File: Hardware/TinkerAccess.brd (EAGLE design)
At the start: 65 x 56.5 mm, 45 parts, among them Q1 500mA/300V, Q2 310mA/60V/1.6Ω, U1 SOIC-8SOIC-8

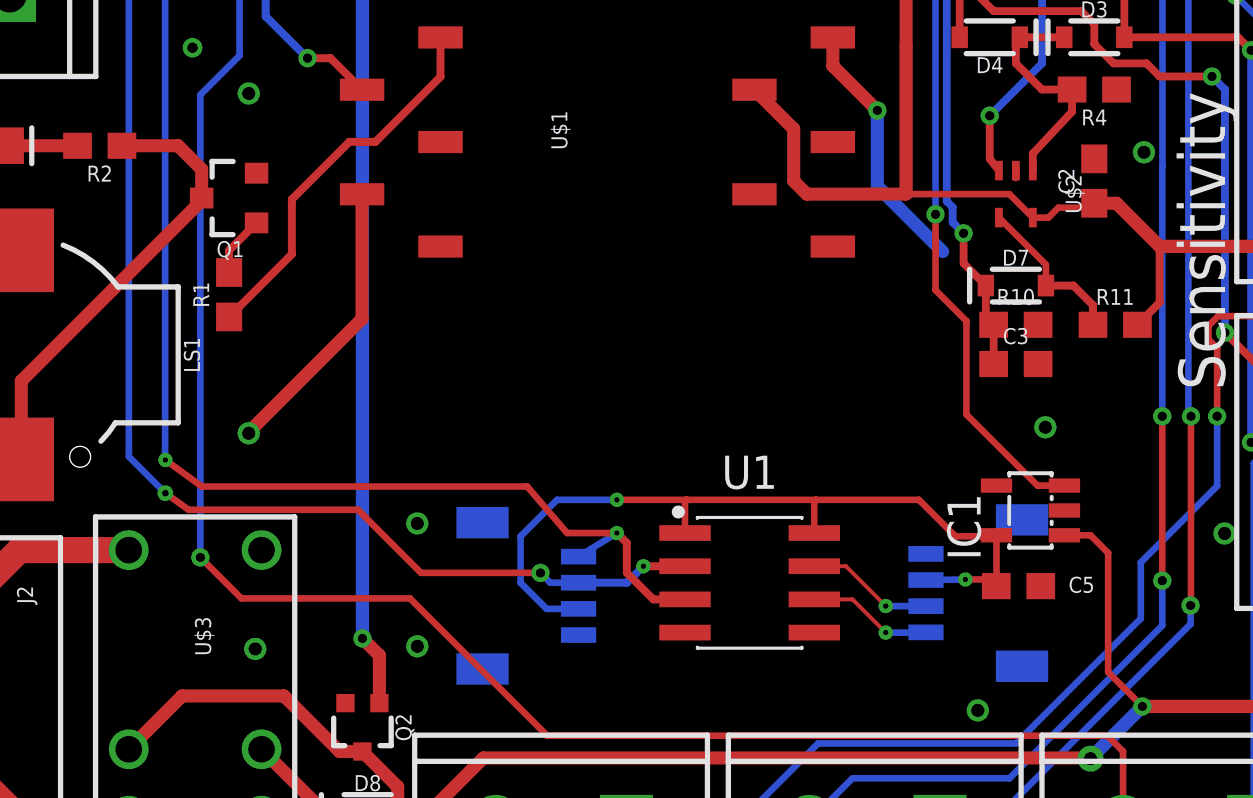
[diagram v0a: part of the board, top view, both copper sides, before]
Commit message: TinkerBoard Update
Fixed Drill Hole size to match Design rules.
Fixed Pad sizes.
Fixed AirWires.
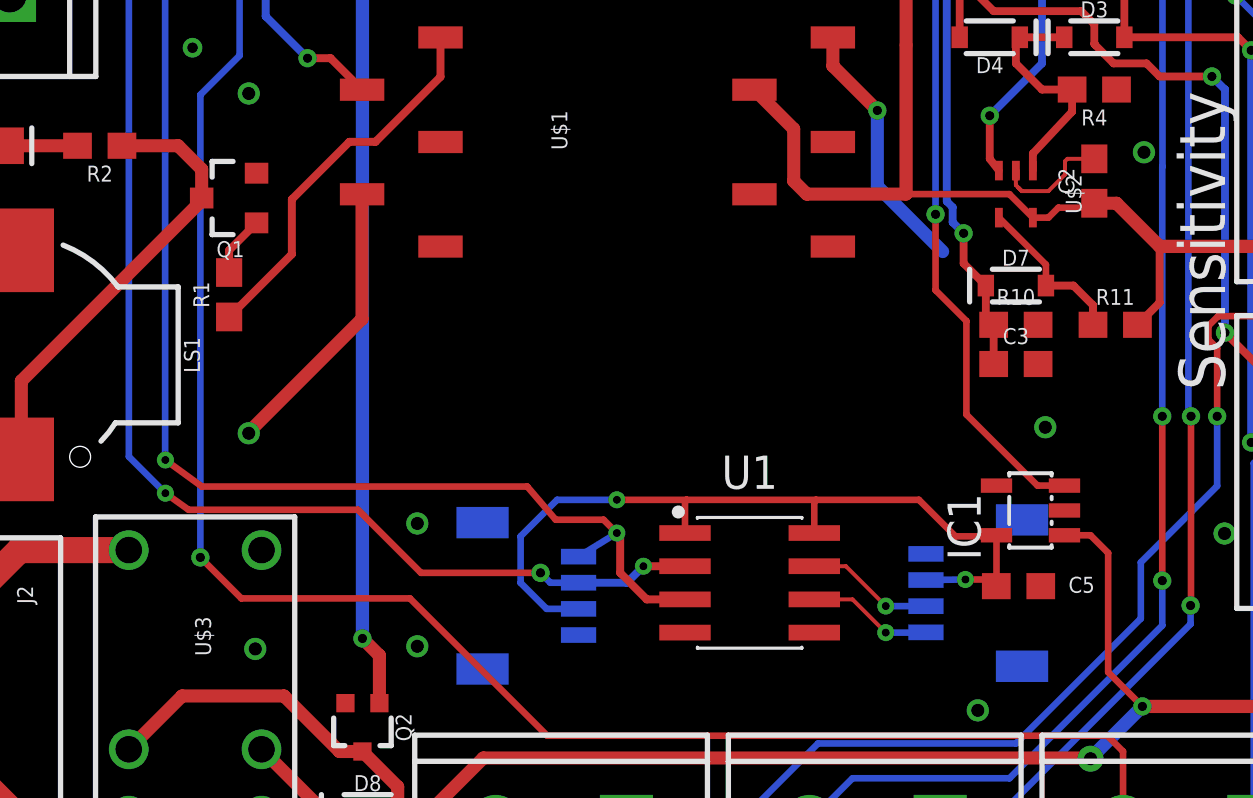
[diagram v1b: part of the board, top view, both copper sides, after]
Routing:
- net GND: track 21.2 -> 25.8 mm
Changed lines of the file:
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@@
 <setting verticaltext="up"/>
 </settings>
-<grid distance="5" unitdist="mil" unit="mil" style="lines" multiple="1" display="no" altdistance="5" altunitdist="mil" altunit="mil"/>
+<grid distance="5" unitdist="mil" unit="mm" style="lines" multiple="1" display="no" altdistance="5" altunitdist="mil" altunit="mm"/>
 <layers>
 <layer number="1" name="Top" color="4" fill="1" visible="yes" active="yes"/>
@@
 </class>
 </classes>
-<designrules name="LaenPCBOrder">
+<designrules name="LaenPCBOrder *">
 <description language="de">&lt;b&gt;EAGLE Design Rules&lt;/b&gt;
 &lt;p&gt;
@@
 <param name="mdSmdStop" value="0mil"/>
 <param name="msWidth" value="6mil"/>
-<param name="msDrill" value="13mil"/>
+<param name="msDrill" value="0.3mm"/>
 <param name="msMicroVia" value="13mil"/>
 <param name="msBlindViaRatio" value="0.5"/>
@@
 <signal name="BSDA">
 <contactref element="J9" pad="3"/>
-<via x="41.021" y="15.24" extent="1-16" drill="0.2"/>
+<via x="41.021" y="15.24" extent="1-16" drill="0.3"/>
 <contactref element="U1" pad="7"/>
 <wire x1="38.2874" y1="16.764" x2="39.497" y2="16.764" width="0.1524" layer="1"/>
@@
 <signal name="BSCL">
 <contactref element="J9" pad="4"/>
-<via x="41.021" y="14.224" extent="1-16" drill="0.2"/>
+<via x="41.021" y="14.224" extent="1-16" drill="0.3"/>
 <wire x1="42.549" y1="14.224" x2="42.56" y2="14.235" width="0.254" layer="16"/>
 <contactref element="U1" pad="6"/>
@@
 <via x="47.1248" y="22.0798" extent="1-16" drill="0.5" diameter="0.55" shape="square"/>
 <contactref element="U1" pad="4"/>
-<wire x1="52.6" y1="45.7" x2="56.63" y2="51.23" width="0" layer="19" extent="1-1"/>
-<wire x1="52.6" y1="44" x2="52.6" y2="45.7" width="0" layer="19" extent="1-1"/>
-<wire x1="52.6" y1="42.3" x2="52.6" y2="44" width="0" layer="19" extent="1-1"/>
-<wire x1="49.85" y1="43" x2="52.6" y2="42.3" width="0" layer="19" extent="1-1"/>
-<wire x1="54.9" y1="40.6" x2="52.6" y2="42.3" width="0" layer="19" extent="1-1"/>
-<wire x1="44.9" y1="45.6" x2="49.85" y2="43" width="0" layer="19" extent="1-1"/>
-<wire x1="49.85" y1="35" x2="54.9" y2="40.6" width="0" layer="19" extent="1-1"/>
-<wire x1="50.9" y1="32.6" x2="49.85" y2="35" width="0" layer="19" extent="1-1"/>
-<wire x1="49" y1="32.35" x2="50.9" y2="32.6" width="0" layer="19" extent="1-1"/>
-<wire x1="46" y1="31.9" x2="49" y2="32.35" width="0" layer="19" extent="1-1"/>
-<wire x1="43.2" y1="28.8" x2="46" y2="31.63979375" width="0" layer="19" extent="1-16"/>
-<wire x1="46.85" y1="26" x2="43.2" y2="28.8" width="0" layer="19" extent="1-16"/>
-<wire x1="46.85" y1="24.5" x2="46.85" y2="26" width="0" layer="19" extent="1-1"/>
-<wire x1="47.1248" y1="22.0798" x2="46.85" y2="24.5" width="0" layer="19" extent="1-1"/>
-<wire x1="47.8583" y1="18.8976" x2="47.1248" y2="22.0798" width="0" layer="19" extent="1-1"/>
-<wire x1="46.951" y1="16.002" x2="47.8583" y2="18.8976" width="0" layer="19" extent="1-1"/>
-<wire x1="42.56" y1="17.235" x2="46.951" y2="16.002" width="0" layer="19" extent="1-16"/>
-<wire x1="44.543" y1="11.249" x2="46.951" y2="16.002" width="0" layer="19" extent="1-1"/>
-<wire x1="53.9828" y1="18.0158" x2="47.8583" y2="18.8976" width="0" layer="19" extent="1-1"/>
-<wire x1="58.9" y1="16.6" x2="53.9828" y2="18.0158" width="0" layer="19" extent="1-1"/>
-<wire x1="60" y1="20" x2="58.9" y2="16.6" width="0" layer="19" extent="1-1"/>
-<wire x1="60.9" y1="24.6" x2="60" y2="20" width="0" layer="19" extent="1-1"/>
-<wire x1="49.01" y1="53.77" x2="56.63" y2="51.23" width="0" layer="19" extent="1-1"/>
-<wire x1="43.93" y1="53.77" x2="49.01" y2="53.77" width="0" layer="19" extent="1-1"/>
-<wire x1="38.85" y1="51.23" x2="43.93" y2="53.77" width="0" layer="19" extent="1-1"/>
-<wire x1="31.23" y1="53.77" x2="38.85" y2="51.23" width="0" layer="19" extent="1-1"/>
-<wire x1="23.61" y1="53.77" x2="31.23" y2="53.77" width="0" layer="19" extent="1-1"/>
-<wire x1="18.53" y1="51.23" x2="23.61" y2="53.77" width="0" layer="19" extent="1-1"/>
-<wire x1="13.45" y1="53.77" x2="18.53" y2="51.23" width="0" layer="19" extent="1-1"/>
-<wire x1="14.9" y1="45.6" x2="18.53" y2="51.23" width="0" layer="19" extent="1-1"/>
-<wire x1="17.35" y1="41" x2="14.9" y2="45.6" width="0" layer="19" extent="1-1"/>
-<wire x1="12.8" y1="40.3" x2="17.35" y2="41" width="0" layer="19" extent="1-1"/>
-<wire x1="14.5" y1="36.6" x2="12.8" y2="40.3" width="0" layer="19" extent="1-1"/>
-<wire x1="16.65" y1="34.85" x2="14.5" y2="36.6" width="0" layer="19" extent="1-1"/>
-<wire x1="16.95" y1="31.8" x2="16.65" y2="34.85" width="0" layer="19" extent="1-1"/>
-<wire x1="20.9868" y1="30.9934" x2="16.95" y2="31.8" width="0" layer="19" extent="1-1"/>
-<wire x1="16.65" y1="21.85" x2="16.6" y2="21.841" width="0" layer="19" extent="1-1"/>
-<wire x1="7.5" y1="38.6" x2="12.8" y2="40.3" width="0" layer="19" extent="1-1"/>
-<wire x1="23.1" y1="18.4" x2="16.65" y2="21.85" width="0" layer="19" extent="1-1"/>
-<wire x1="23.1" y1="13.7" x2="23.1" y2="18.4" width="0" layer="19" extent="1-1"/>
-<wire x1="20.35" y1="11.525" x2="23.1" y2="13.7" width="0" layer="19" extent="1-1"/>
-<wire x1="16.9" y1="13.6" x2="20.35" y2="11.525" width="0" layer="19" extent="1-1"/>
-<wire x1="29.2688" y1="14.1318" x2="23.1" y2="13.7" width="0" layer="19" extent="16-16"/>
-<wire x1="33.3406" y1="14.224" x2="29.2688" y2="14.1318" width="0" layer="19" extent="1-16"/>
-<wire x1="26.1" y1="7" x2="20.35" y2="11.525" width="0" layer="19" extent="1-1"/>
-<wire x1="4.7" y1="45.5" x2="7.5" y2="38.6" width="0" layer="19" extent="1-1"/>
-<wire x1="39.563" y1="4.331" x2="44.543" y2="11.249" width="0" layer="19" extent="1-1"/>
-<wire x1="61.9" y1="34.6" x2="54.9" y2="40.6" width="0" layer="19" extent="1-1"/>
-<wire x1="4.55" y1="23.95" x2="16.6" y2="21.841" width="0" layer="19" extent="1-1"/>
-<wire x1="8.8" y1="2.9" x2="16.9" y2="13.6" width="0" layer="19" extent="1-1"/>
+<wire x1="46" y1="31.343" x2="46.101" y2="31.242" width="0.1524" layer="1"/>
+<wire x1="46.101" y1="31.242" x2="46.228" y2="31.115" width="0.1524" layer="1"/>
+<wire x1="46" y1="31.9" x2="46" y2="31.343" width="0.1524" layer="1"/>
+<wire x1="46.101" y1="31.242" x2="46.228" y2="31.115" width="0.1524" layer="1"/>
+<wire x1="46.228" y1="31.115" x2="47.244" y2="31.115" width="0.1524" layer="1"/>
+<wire x1="47.244" y1="31.115" x2="47.879" y2="31.75" width="0.1524" layer="1"/>
+<wire x1="47.879" y1="31.75" x2="47.879" y2="32.258" width="0.1524" layer="1"/>
+<wire x1="47.879" y1="32.258" x2="47.971" y2="32.35" width="0.1524" layer="1"/>
+<wire x1="47.971" y1="32.35" x2="49" y2="32.35" width="0.1524" layer="1"/>
 </signal>
 <signal name="TXD">
@@
 <wire x1="45.2581" y1="16.256" x2="45.2581" y2="16.0091" width="0.254" layer="1"/>
 <wire x1="45.2581" y1="16.0091" x2="45.251" y2="16.002" width="0.254" layer="1"/>
-<via x="44.069" y="16.256" extent="1-16" drill="0.2"/>
+<via x="44.069" y="16.256" extent="1-16" drill="0.3"/>
 <wire x1="44.069" y1="16.256" x2="42.56" y2="16.235" width="0.254" layer="16"/>
 <wire x1="44.069" y1="16.256" x2="45.2581" y2="16.256" width="0.254" layer="1"/>
-<via x="30.734" y="19.304" extent="1-16" drill="0.2"/>
+<via x="30.734" y="19.304" extent="1-16" drill="0.3"/>
 <wire x1="30.734" y1="19.304" x2="28.448" y2="19.304" width="0.254" layer="16"/>
 <wire x1="28.448" y1="19.304" x2="27.051" y2="17.907" width="0.254" layer="16"/>
@@
 <contactref element="J8" pad="3"/>
 <contactref element="RPI1" pad="3"/>
-<via x="31.75" y="16.764" extent="1-16" drill="0.2"/>
+<via x="31.75" y="16.764" extent="1-16" drill="0.3"/>
 <wire x1="10.91" y1="51.23" x2="10.91" y2="46.494" width="0.254" layer="16"/>
 <wire x1="10.91" y1="46.494" x2="12.065" y2="45.339" width="0.254" layer="16"/>
 <wire x1="12.065" y1="45.339" x2="12.065" y2="20.955" width="0.254" layer="16"/>
 <wire x1="12.065" y1="20.955" x2="13.462" y2="19.558" width="0.254" layer="16"/>
-<via x="13.462" y="19.558" extent="1-16" drill="0.25"/>
+<via x="13.462" y="19.558" extent="1-16" drill="0.3"/>
 <wire x1="13.462" y1="19.558" x2="14.351" y2="18.923" width="0.254" layer="1"/>
 <wire x1="14.351" y1="18.923" x2="20.828" y2="18.923" width="0.254" layer="1"/>
@@
 <wire x1="13.45" y1="20.84" x2="13.462" y2="20.828" width="0.254" layer="16"/>
 <wire x1="29.2688" y1="17.1318" x2="30.734" y2="18.034" width="0.254" layer="16"/>
-<via x="13.462" y="20.828" extent="1-16" drill="0.2"/>
+<via x="13.462" y="20.828" extent="1-16" drill="0.3"/>
 <wire x1="13.462" y1="20.828" x2="14.859" y2="19.812" width="0.254" layer="1"/>
-<via x="30.734" y="18.034" extent="1-16" drill="0.2"/>
+<via x="30.734" y="18.034" extent="1-16" drill="0.3"/>
 <wire x1="14.859" y1="19.812" x2="27.305" y2="19.812" width="0.254" layer="1"/>
-<wire x1="27.305" y1="19.812" x2="28.829" y2="18.034" width="0.254" layer="1"/>
-<wire x1="28.829" y1="18.034" x2="30.734" y2="18.034" width="0.254" layer="1"/>
+<wire x1="27.305" y1="19.812" x2="28.393571875" y2="18.542" width="0.254" layer="1"/>
+<wire x1="30.226" y1="18.542" x2="28.393571875" y2="18.542" width="0.254" layer="1"/>
+<wire x1="30.226" y1="18.542" x2="30.734" y2="18.034" width="0.254" layer="1"/>
 <contactref element="U1" pad="3"/>
-<wire x1="33.3406" y1="15.494" x2="32.131" y2="15.494" width="0.3048" layer="1"/>
-<wire x1="31.115" y1="16.51" x2="32.131" y2="15.494" width="0.3048" layer="1"/>
-<wire x1="30.734" y1="18.034" x2="31.115" y2="17.653" width="0.3048" layer="1"/>
-<wire x1="31.115" y1="17.653" x2="31.115" y2="16.51" width="0.3048" layer="1"/>
+<wire x1="33.3406" y1="15.494" x2="31.877" y2="15.494" width="0.3048" layer="1"/>
+<wire x1="30.861" y1="16.51" x2="31.877" y2="15.494" width="0.3048" layer="1"/>
+<wire x1="30.734" y1="18.034" x2="30.861" y2="17.907" width="0.3048" layer="1"/>
+<wire x1="30.861" y1="17.907" x2="30.861" y2="16.51" width="0.3048" layer="1"/>
 </signal>
 <signal name="N$8">

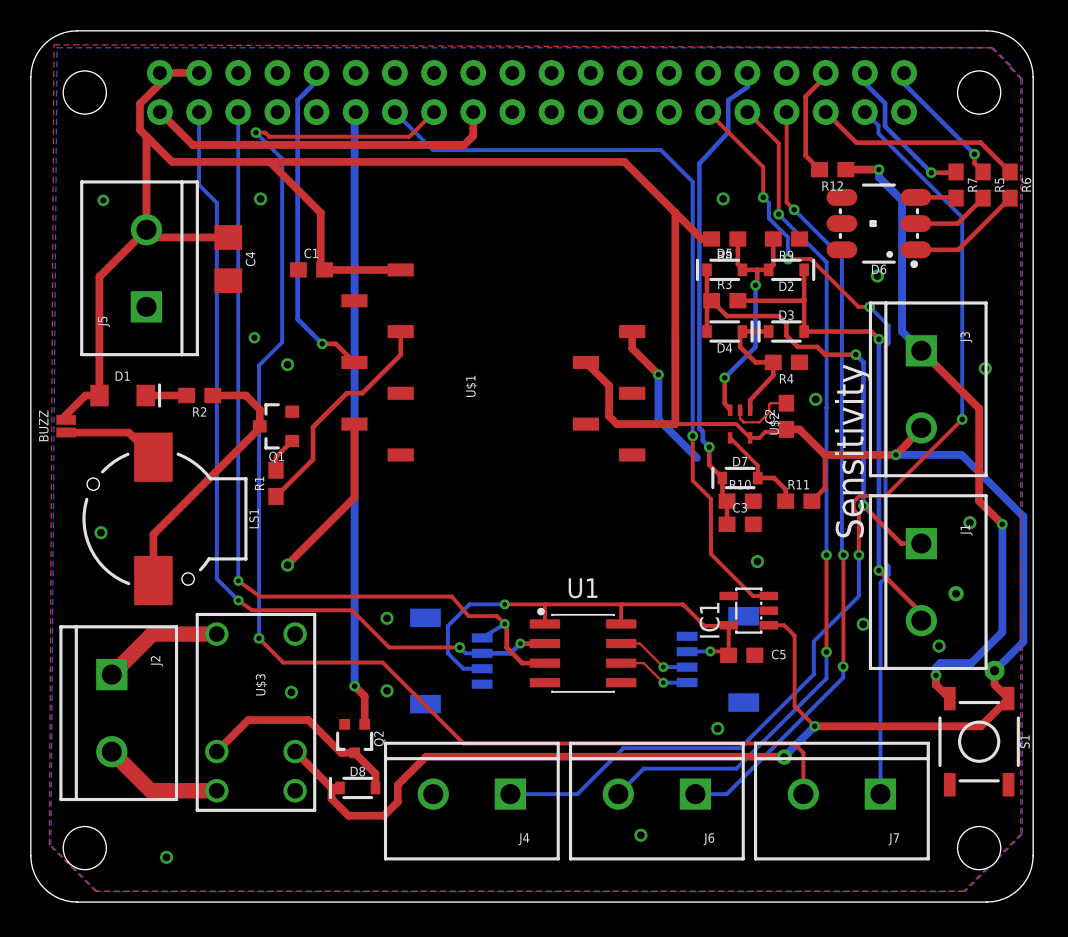
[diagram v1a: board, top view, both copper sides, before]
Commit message: added pulldown
Added pulldown resistor to 3v3 Enable line
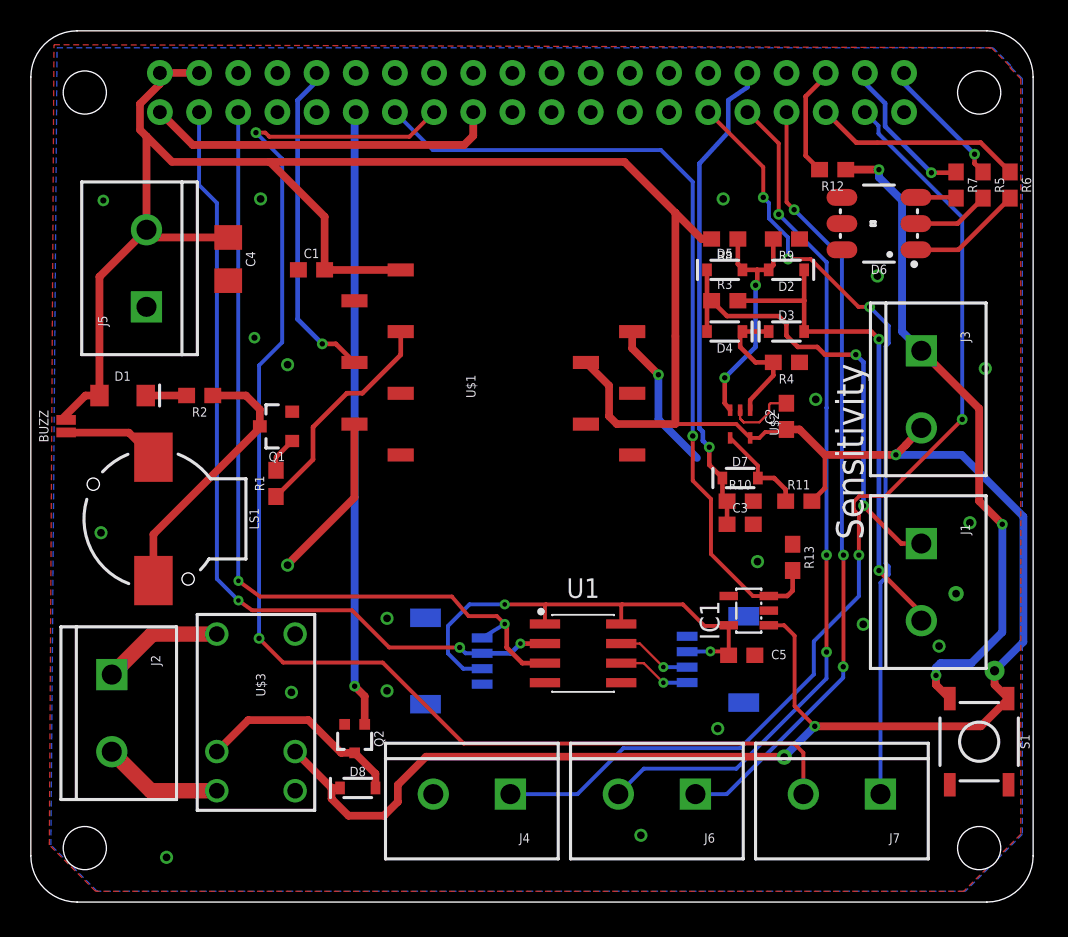
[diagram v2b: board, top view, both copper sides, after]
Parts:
- added R13: 10k, SparkFun-Resistors:0603
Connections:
- net 3.3V_EN: now also R13.2
- net GND: now also R13.1
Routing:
- net 3.3V_EN: track 50.7 -> 53.7 mm
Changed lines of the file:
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@@
 <attribute name="VALUE" x="3.429" y="30.861" size="0.6096" layer="27" font="vector" ratio="20" rot="R90" align="top-center"/>
+</element>
+<element name="R13" library="SparkFun-Resistors" library_urn="urn:adsk.eagle:library:532" package="0603" package3d_urn="urn:adsk.eagle:package:39650/1" value="10k" x="49.403" y="22.352" smashed="yes" rot="R270">
+<attribute name="NAME" x="50.165" y="22.352" size="0.6096" layer="25" font="vector" ratio="20" rot="R270" align="bottom-center"/>
+<attribute name="PROD_ID" value="RES-00824" x="49.403" y="22.352" size="1.778" layer="27" rot="R270" display="off"/>
+<attribute name="VALUE" x="48.641" y="22.352" size="0.6096" layer="27" font="vector" ratio="20" rot="R270" align="top-center"/>
 </element>
 </elements>
@@
 <wire x1="47.879" y1="32.258" x2="47.971" y2="32.35" width="0.1524" layer="1"/>
 <wire x1="47.971" y1="32.35" x2="49" y2="32.35" width="0.1524" layer="1"/>
+<contactref element="R13" pad="1"/>
 </signal>
 <signal name="TXD">
@@
 <wire x1="41.8" y1="36.7" x2="41.8" y2="44.7" width="0.5" layer="1"/>
 <wire x1="15.5" y1="48" x2="9.1572" y2="48" width="0.5" layer="1"/>
-<wire x1="15.5" y1="48" x2="18.8" y2="44.7" width="0.5" layer="1"/>
-<wire x1="18.8" y1="44.7" x2="18.8" y2="41.25" width="0.5" layer="1"/>
-<wire x1="19.05" y1="41" x2="18.8" y2="41.25" width="0.5" layer="1"/>
+<wire x1="15.5" y1="48" x2="19.054" y2="44.446" width="0.5" layer="1"/>
+<wire x1="19.054" y1="44.446" x2="19.054" y2="41.004" width="0.5" layer="1"/>
+<wire x1="19.05" y1="41" x2="19.054" y2="41.004" width="0.5" layer="1"/>
 <wire x1="23.9868" y1="40.9934" x2="19.0566" y2="40.9934" width="0.5" layer="1"/>
 <wire x1="19.0566" y1="40.9934" x2="19.05" y2="41" width="0.5" layer="1"/>
@@
 <wire x1="26.072" y1="48.768" x2="40.8651625" y2="48.768" width="0.254" layer="16"/>
 <wire x1="44.1072" y1="22.5678" x2="46.8274" y2="19.8476" width="0.254" layer="1"/>
+<contactref element="R13" pad="2"/>
+<wire x1="49.403" y1="21.502" x2="49.403" y2="20.193" width="0.3048" layer="1"/>
+<wire x1="49.0576" y1="19.8476" x2="47.8583" y2="19.8476" width="0.3048" layer="1"/>
+<wire x1="49.403" y1="20.193" x2="49.0576" y2="19.8476" width="0.3048" layer="1"/>
 </signal>
 </signals>
